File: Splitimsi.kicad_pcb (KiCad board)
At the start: 2 copper layers, 118.2 x 100.1 mm, 34 parts, among them SW1 MX_RGB, SW10 MX_RGB, SW11 MX_RGB, SW12 MX_RGB, SW13 MX_RGB, SW14 MX_RGB, SW15 MX_RGB, SW16 MX_RGB, SW17 MX_RGB, SW18 MX_RGB, SW19 MX_RGB, SW2 MX_RGB, SW20 MX_RGB, SW21 MX_RGB, SW22 MX_RGB, SW23 MX_RGB, SW24 MX_RGB, SW25 MX_RGB, SW26 MX_RGB, SW27 MX_RGB, SW3 MX_RGB, SW4 MX_RGB, SW5 MX_RGB, SW6 MX_RGB, SW7 MX_RGB, SW8 MX_RGB, SW9 MX_RGB, U1 ProMicro, U2 TRRS

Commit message: Knob added to sw annotations
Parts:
- renumbered Knob1 to SW16, SW16 to SW17, SW17 to SW18, SW18 to SW19, SW19 to SW20, SW20 to SW21, SW21 to SW22, SW22 to SW23, SW23 to SW24, SW24 to SW25, SW25 to SW26, SW26 to SW27, SW27 to SW28
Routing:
- net +5V: track 595.2 -> 601.9 mm

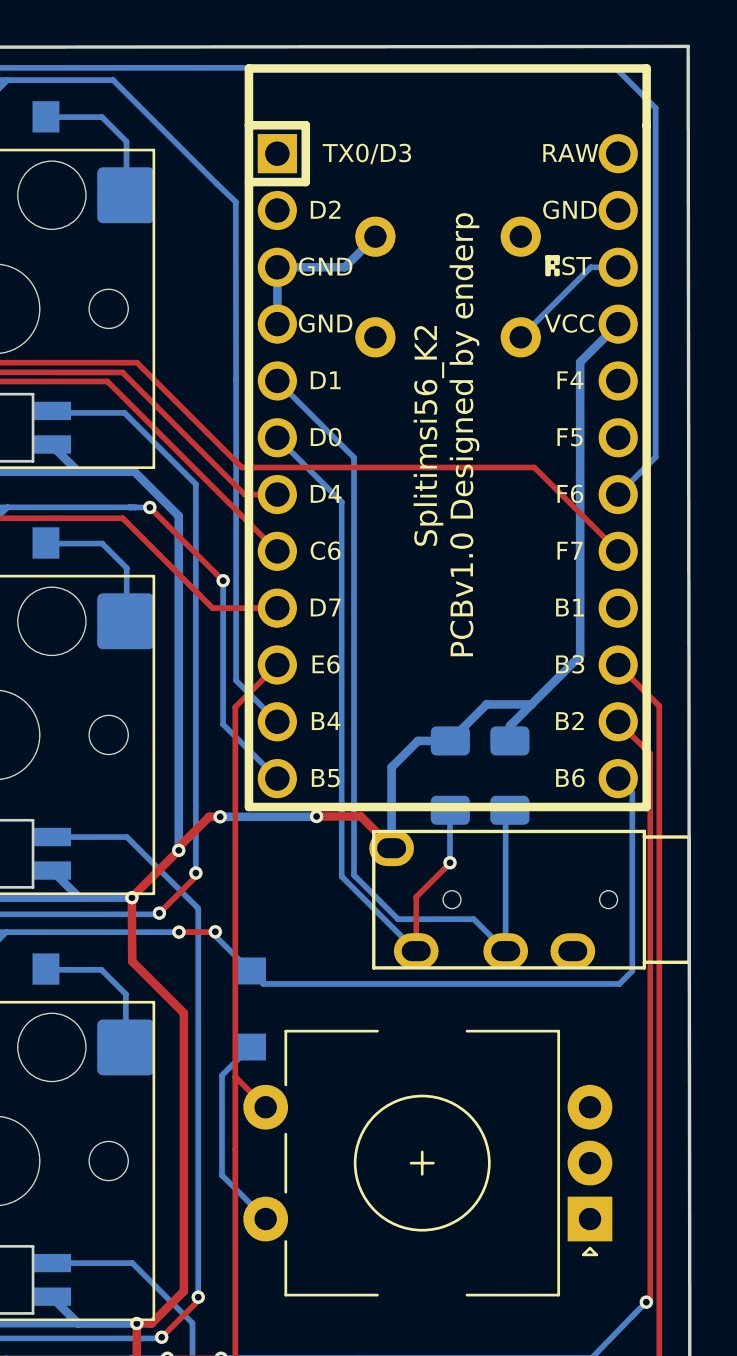
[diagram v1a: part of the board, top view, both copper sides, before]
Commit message: Reset switch sch and footprint fucked
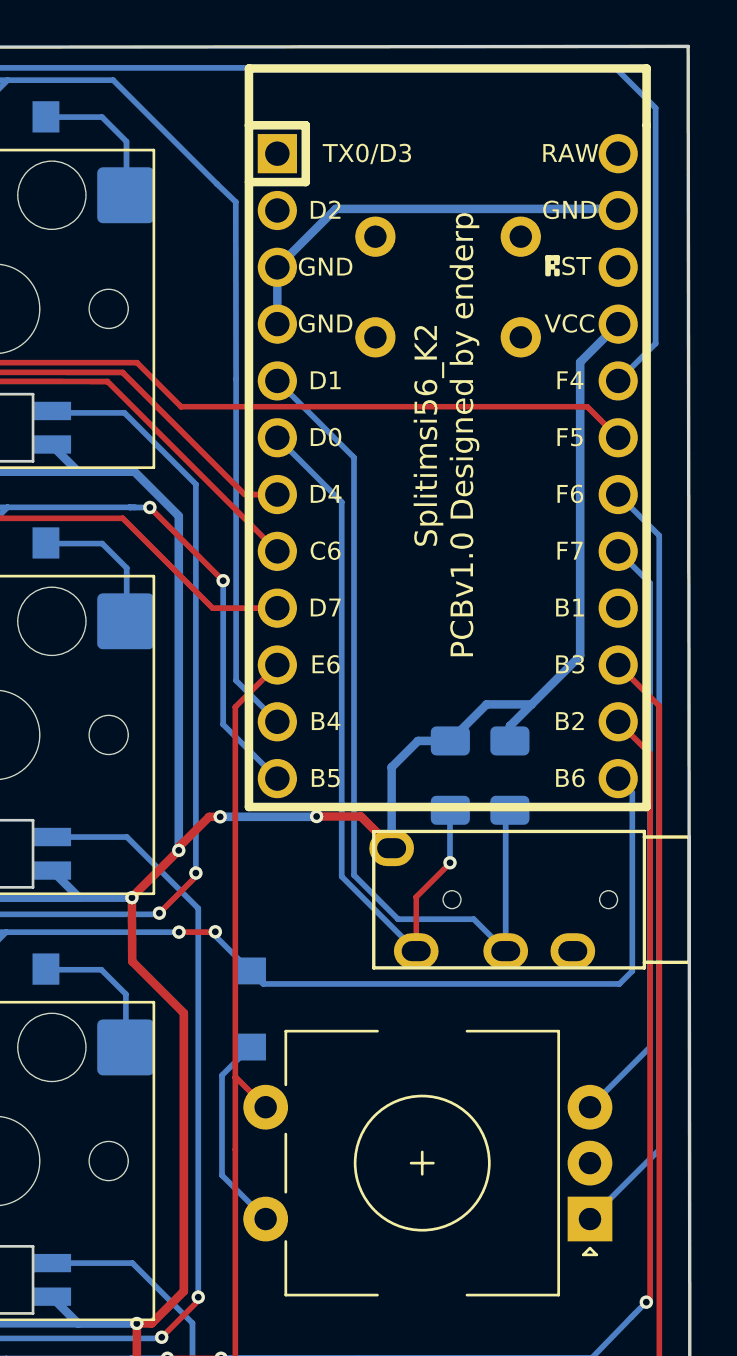
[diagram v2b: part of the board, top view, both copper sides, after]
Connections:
- S1 pad 1: GND -> unconnected-(S1-Pad1)
- S1 pad 2: Net-(S1-Pad2)_1 -> unconnected-(S1-Pad2)
- SW16 pad A: unconnected-(SW16-PadA) -> /RotPinA
- SW16 pad B: unconnected-(SW16-PadB) -> /RotPinB
- SW16 pad C: unconnected-(SW16-PadC) -> GND
- U1 pad 17: /Col1 -> /RotPinB
- U1 pad 18: /Col0 -> /RotPinA
- U1 pad 19: unconnected-(U1-Pad19) -> /Col1
- U1 pad 20: unconnected-(U1-Pad20) -> /Col0
- U1 pad 22: Net-(S1-Pad2)_1 -> unconnected-(U1-Pad22)
- U1 pad 23: Net-(S1-Pad1) -> GND
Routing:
- net /RotPinA: track 0.00 -> 34.4 mm
- net /RotPinB: track 0.00 -> 26.6 mm
- net GND: track 7.49 -> 18.9 mm
- net Net-(S1-Pad2)_1: track 5.65 -> 0.00 mm
- net /Col0: track 224.0 -> 219.0 mm
- net /Col1: track 184.1 -> 182.0 mm

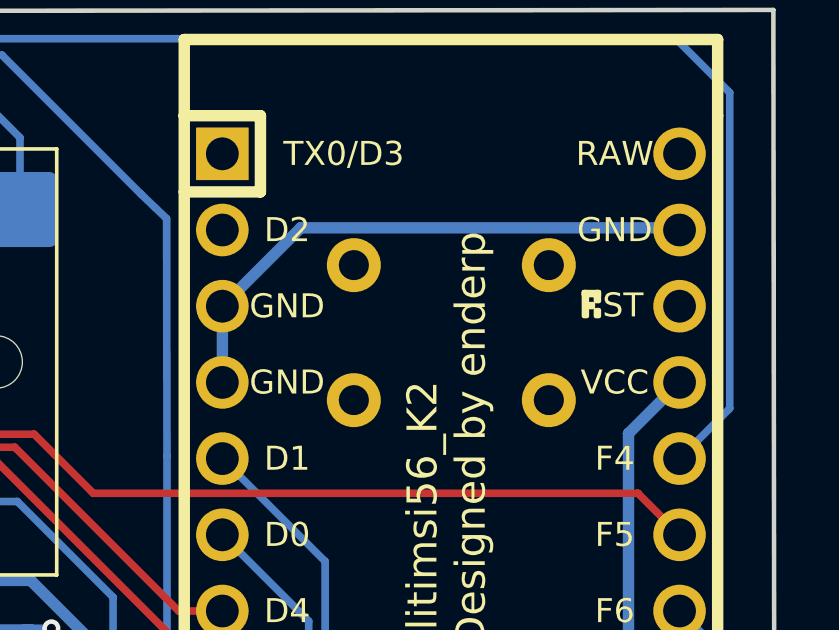
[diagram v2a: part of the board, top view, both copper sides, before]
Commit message: Reset button fixed
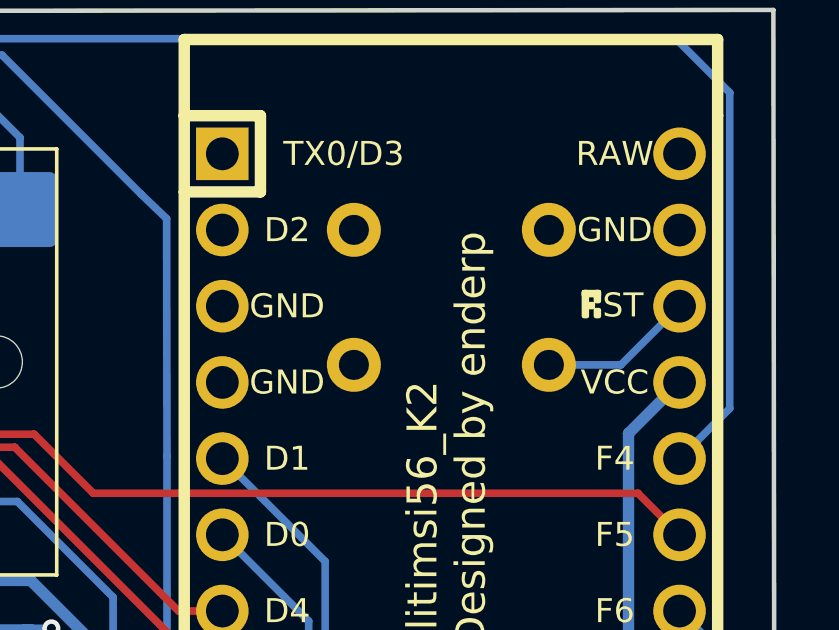
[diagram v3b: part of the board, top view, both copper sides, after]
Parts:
- moved S1 1.18 mm to (127.6, 26.4)
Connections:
- S1 pad 1: unconnected-(S1-Pad1) -> GND
- S1 pad 2: unconnected-(S1-Pad2) -> Net-(S1-Pad2)_1
- U1 pad 22: unconnected-(U1-Pad22) -> Net-(S1-Pad2)_1
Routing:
- net GND: track 18.9 -> 0.10 mm
- net Net-(S1-Pad2)_1: track 0.00 -> 5.17 mm
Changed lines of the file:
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@@
   (net 67 "/RotPinB")
   (net 68 "/Row1")
-  (net 69 "unconnected-(S1-Pad2)")
+  (net 69 "Net-(S1-Pad2)_1")
   (net 70 "/Row3")
   (net 71 "unconnected-(U1-Pad24)")
@@
   (net 73 "/SCL")
   (net 74 "/Row4_LedOut")
-  (net 75 "unconnected-(U1-Pad22)")
-  (net 76 "Net-(SW21-Pad4)")
-  (net 77 "Net-(SW27-Pad4)")
-  (net 78 "Net-(SW28-Pad2)")
-  (net 79 "unconnected-(S1-Pad1)")
+  (net 75 "Net-(SW21-Pad4)")
+  (net 76 "Net-(SW27-Pad4)")
+  (net 77 "Net-(SW28-Pad2)")
   (footprint "KeyboardCustomFPs:Kailh_HS_MX_LED" (layer "F.Cu")
     (at 107.95 85.725)
@@
       (net 3 "+5V") (pinfunction "VDD") (pintype "power_in"))
     (pad "4" smd rect (at 1.913633 4.564178) (size 1.7 0.82) (layers "B.Cu" "B.Paste" "B.Mask")
-      (net 76 "Net-(SW21-Pad4)") (pinfunction "DOUT") (pintype "output"))
+      (net 75 "Net-(SW21-Pad4)") (pinfunction "DOUT") (pintype "output"))
     (pad "5" smd roundrect (at -3.186367 4.564178) (size 1.7 0.82) (layers "B.Cu" "B.Paste" "B.Mask") (roundrect_rratio 0.25)
       (net 5 "GND") (pinfunction "GND") (pintype "power_in"))
@@
       (net 5 "GND") (pinfunction "GND") (pintype "power_in"))
     (pad "6" smd rect (at -3.186367 6.064178) (size 1.7 0.82) (layers "B.Cu" "B.Paste" "B.Mask")
-      (net 76 "Net-(SW21-Pad4)") (pinfunction "DIN") (pintype "input"))
+      (net 75 "Net-(SW21-Pad4)") (pinfunction "DIN") (pintype "input"))
     (pad "7" smd rect (at -1.759961 -8.583285 180) (size 1.2 1.4) (layers "B.Cu" "B.Paste" "B.Mask")
       (net 70 "/Row3") (pinfunction "K") (pintype "passive"))
@@
       (net 3 "+5V") (pinfunction "VCC") (pintype "input"))
     (pad "22" thru_hole circle (at -8.89 -7.62 270) (size 1.7526 1.7526) (drill 1.0922) (layers *.Cu *.SilkS *.Mask)
-      (net 75 "unconnected-(U1-Pad22)") (pinfunction "RST") (pintype "input"))
+      (net 69 "Net-(S1-Pad2)_1") (pinfunction "RST") (pintype "input"))
     (pad "23" thru_hole circle (at -11.43 -7.62 270) (size 1.7526 1.7526) (drill 1.0922) (layers *.Cu *.SilkS *.Mask)
       (net 5 "GND") (pinfunction "GND") (pintype "input"))
@@
       (net 3 "+5V") (pinfunction "VDD") (pintype "power_in"))
     (pad "4" smd rect (at 1.913633 4.564178) (size 1.7 0.82) (layers "B.Cu" "B.Paste" "B.Mask")
-      (net 77 "Net-(SW27-Pad4)") (pinfunction "DOUT") (pintype "output"))
+      (net 76 "Net-(SW27-Pad4)") (pinfunction "DOUT") (pintype "output"))
     (pad "5" smd roundrect (at -3.186367 4.564178) (size 1.7 0.82) (layers "B.Cu" "B.Paste" "B.Mask") (roundrect_rratio 0.25)
       (net 5 "GND") (pinfunction "GND") (pintype "power_in"))
@@
       (net 7 "/Col5") (pintype "passive"))
     (pad "2" smd roundrect (at 5.207 -5.08) (size 2.55 2.5) (layers "B.Cu" "B.Paste" "B.Mask") (roundrect_rratio 0.1)
-      (net 78 "Net-(SW28-Pad2)") (pintype "passive"))
+      (net 77 "Net-(SW28-Pad2)") (pintype "passive"))
     (pad "3" smd rect (at 1.913633 6.064178) (size 1.7 0.82) (layers "B.Cu" "B.Paste" "B.Mask")
       (net 3 "+5V") (pinfunction "VDD") (pintype "power_in"))
@@
       (net 5 "GND") (pinfunction "GND") (pintype "power_in"))
     (pad "6" smd rect (at -3.186367 6.064178) (size 1.7 0.82) (layers "B.Cu" "B.Paste" "B.Mask")
-      (net 77 "Net-(SW27-Pad4)") (pinfunction "DIN") (pintype "input"))
+      (net 76 "Net-(SW27-Pad4)") (pinfunction "DIN") (pintype "input"))
     (pad "7" smd rect (at -1.759961 -8.583285 180) (size 1.2 1.4) (layers "B.Cu" "B.Paste" "B.Mask")
       (net 72 "/Row4") (pinfunction "K") (pintype "passive"))
     (pad "8" smd rect (at 1.640039 -8.583285 180) (size 1.2 1.4) (layers "B.Cu" "B.Paste" "B.Mask")
-      (net 78 "Net-(SW28-Pad2)") (pinfunction "A") (pintype "passive"))
+      (net 77 "Net-(SW28-Pad2)") (pinfunction "A") (pintype "passive"))
     (model "${KICAD6_3RD_PARTY}/3dmodels/keebio/SK6812MINI-E v1.step"
       (offset (xyz -0.6 -5.27 -1.8))
@@
   )
   (footprint "aio3-misc:PushButton_6x6mm_TH_Pretty" (layer "B.Cu")
-    (at 127.569604 27.597679 180)
+    (at 127.570436 26.422467 180)
     (property "Sheetfile" "Splitimsi.kicad_sch")
     (property "Sheetname" "")
@@
     (fp_circle (center 0 0) (end 1.27 1.27) (layer "B.SilkS") (width 0.15) (fill none))
     (pad "1" thru_hole circle (at -3.25 2.25 180) (size 1.8 1.8) (drill 1) (layers *.Cu "F.Mask")
-      (net 79 "unconnected-(S1-Pad1)") (pintype "passive"))
+      (net 5 "GND") (pintype "passive"))
     (pad "1" thru_hole circle (at 3.25 2.25 180) (size 1.8 1.8) (drill 1) (layers *.Cu "F.Mask")
-      (net 79 "unconnected-(S1-Pad1)") (pintype "passive"))
+      (net 5 "GND") (pintype "passive"))
     (pad "2" thru_hole circle (at -3.25 -2.25 180) (size 1.8 1.8) (drill 1) (layers *.Cu "F.Mask")
-      (net 69 "unconnected-(S1-Pad2)") (pintype "passive"))
+      (net 69 "Net-(S1-Pad2)_1") (pintype "passive"))
     (pad "2" thru_hole circle (at 3.25 -2.25 180) (size 1.8 1.8) (drill 1) (layers *.Cu "F.Mask")
-      (net 69 "unconnected-(S1-Pad2)") (pintype "passive"))
+      (net 69 "Net-(S1-Pad2)_1") (pintype "passive"))
     (model "${KICAD6_3RD_PARTY}/3dmodels/kicad/Button_Switch_THT.3dshapes/SW_PUSH_6mm.step"
       (offset (xyz -3.2 2.25 0))
@@
   (segment (start 41.455293 34.639178) (end 47.613633 34.639178) (width 0.254) (layer "B.Cu") (net 4))
   (segment (start 39.955293 33.139178) (end 41.455293 34.639178) (width 0.254) (layer "B.Cu") (net 4))
-  (segment (start 119.936143 26.716985) (end 119.936143 29.256985) (width 0.381) (layer "B.Cu") (net 5))
   (segment (start 135.104426 24.105268) (end 135.176143 24.176985) (width 0.381) (layer "B.Cu") (net 5))
-  (segment (start 122.54786 24.105268) (end 135.104426 24.105268) (width 0.381) (layer "B.Cu") (net 5))
-  (segment (start 119.936143 26.716985) (end 122.54786 24.105268) (width 0.381) (layer "B.Cu") (net 5))
   (segment (start 118.05644 46.376688) (end 119.936143 44.496985) (width 0.254) (layer "F.Cu") (net 7))
   (segment (start 118.074518 62.929483) (end 118.05644 62.929483) (width 0.254) (layer "F.Cu") (net 7))
@@
   (segment (start 87.136637 39.079721) (end 88.768329 37.448029) (width 0.254) (layer "B.Cu") (net 68))
   (segment (start 113.338201 37.454517) (end 113.331713 37.448029) (width 0.254) (layer "B.Cu") (net 68))
+  (segment (start 135.176143 26.716985) (end 133.220661 28.672467) (width 0.254) (layer "B.Cu") (net 69))
+  (segment (start 133.220661 28.672467) (end 130.820436 28.672467) (width 0.254) (layer "B.Cu") (net 69))
   (segment (start 136.567518 72.850428) (end 136.433289 72.984657) (width 0.254) (layer "F.Cu") (net 70))
   (segment (start 136.606269 72.850428) (end 136.567518 72.850428) (width 0.254) (layer "F.Cu") (net 70))
@@
   (segment (start 126.145517 57.289572) (end 122.814264 53.958319) (width 0.254) (layer "B.Cu") (net 73))
   (segment (start 122.814264 53.958319) (end 122.814264 37.215106) (width 0.254) (layer "B.Cu") (net 73))
-  (segment (start 116.148759 90.31464) (end 117.648759 91.81464) (width 0.254) (layer "B.Cu") (net 76))
-  (segment (start 109.857099 90.31464) (end 116.148759 90.31464) (width 0.254) (layer "B.Cu") (net 76))
-  (segment (start 117.648759 91.81464) (end 123.807099 91.81464) (width 0.254) (layer "B.Cu") (net 76))
-  (segment (start 117.710206 110.894091) (end 123.868546 110.894091) (width 0.254) (layer "B.Cu") (net 77))
-  (segment (start 109.918546 109.394091) (end 116.210206 109.394091) (width 0.254) (layer "B.Cu") (net 77))
-  (segment (start 116.210206 109.394091) (end 117.710206 110.894091) (width 0.254) (layer "B.Cu") (net 77))
-  (segment (start 128.671835 96.28974) (end 131.14448 96.28974) (width 0.254) (layer "B.Cu") (net 78))
-  (segment (start 132.238796 97.384056) (end 132.238796 99.793025) (width 0.254) (layer "B.Cu") (net 78))
-  (segment (start 131.14448 96.28974) (end 132.238796 97.384056) (width 0.254) (layer "B.Cu") (net 78))
+  (segment (start 116.148759 90.31464) (end 117.648759 91.81464) (width 0.254) (layer "B.Cu") (net 75))
+  (segment (start 109.857099 90.31464) (end 116.148759 90.31464) (width 0.254) (layer "B.Cu") (net 75))
+  (segment (start 117.648759 91.81464) (end 123.807099 91.81464) (width 0.254) (layer "B.Cu") (net 75))
+  (segment (start 117.710206 110.894091) (end 123.868546 110.894091) (width 0.254) (layer "B.Cu") (net 76))
+  (segment (start 109.918546 109.394091) (end 116.210206 109.394091) (width 0.254) (layer "B.Cu") (net 76))
+  (segment (start 116.210206 109.394091) (end 117.710206 110.894091) (width 0.254) (layer "B.Cu") (net 76))
+  (segment (start 128.671835 96.28974) (end 131.14448 96.28974) (width 0.254) (layer "B.Cu") (net 77))
+  (segment (start 132.238796 97.384056) (end 132.238796 99.793025) (width 0.254) (layer "B.Cu") (net 77))
+  (segment (start 131.14448 96.28974) (end 132.238796 97.384056) (width 0.254) (layer "B.Cu") (net 77))
 )

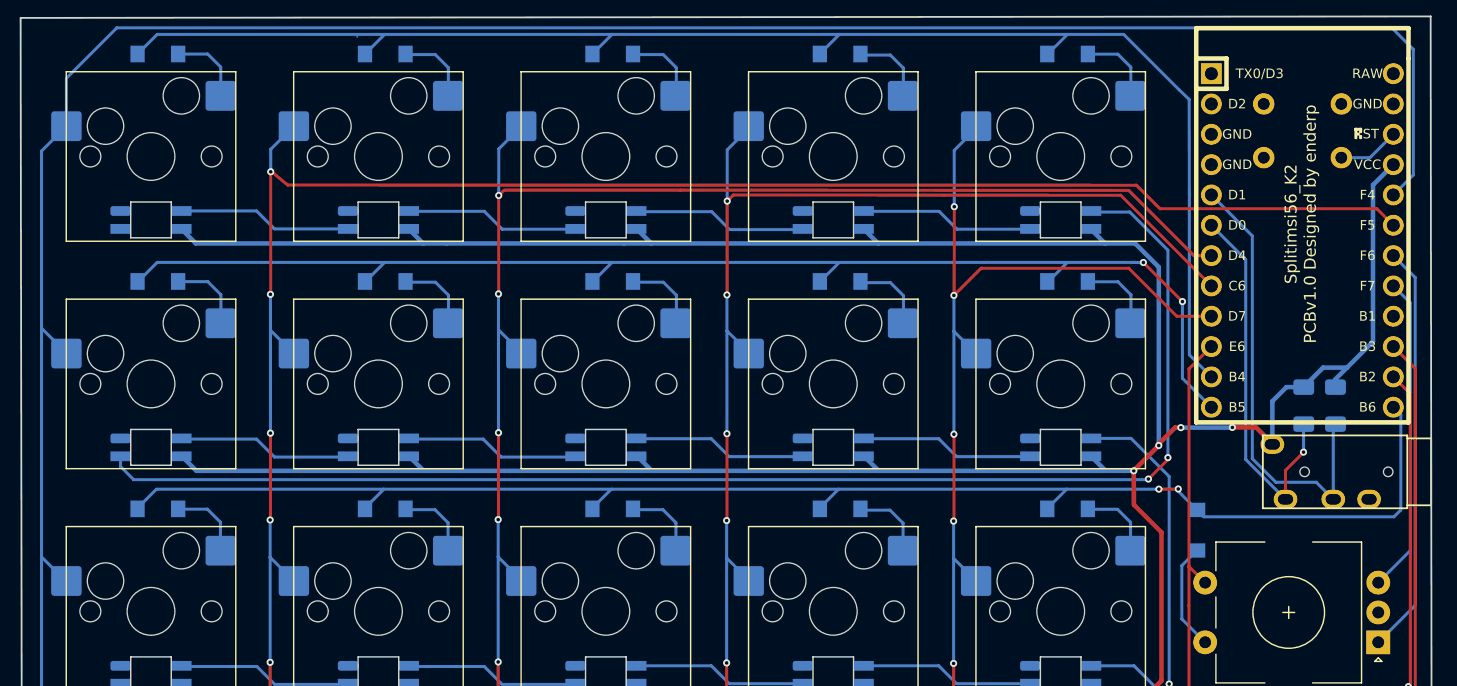
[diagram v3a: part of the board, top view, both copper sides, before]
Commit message: Reset button footprint finalized
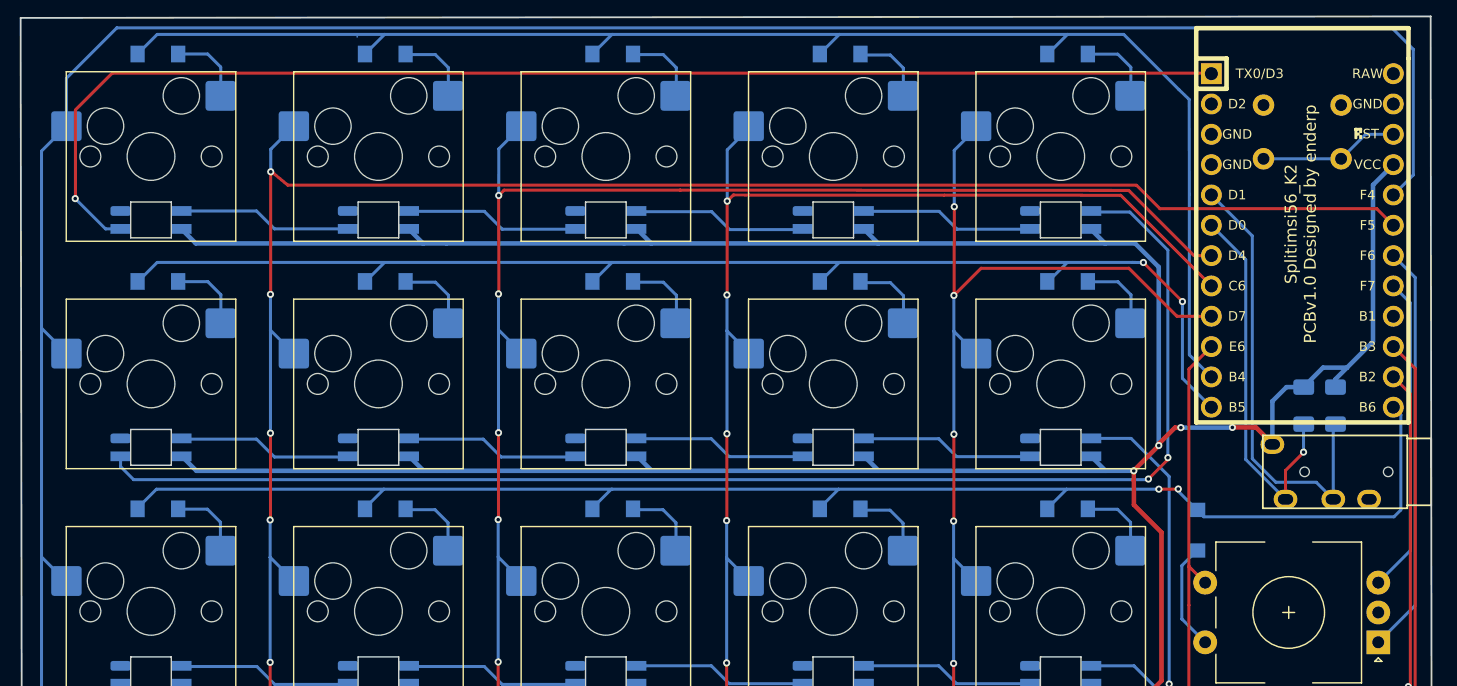
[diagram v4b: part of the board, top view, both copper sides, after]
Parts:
- moved S1 0.10 mm to (127.6, 26.5)
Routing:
- net /LedData: track 0.00 -> 108.8 mm, vias 0 -> 1
- net Net-(S1-Pad2): track 5.17 -> 11.7 mm
